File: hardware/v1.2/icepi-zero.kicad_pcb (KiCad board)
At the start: 4 copper layers, 65 x 30 mm, 158 parts, among them J1 Conn_02x20_Counter_Clockwise, J2 HDMI_C_1.3, J3 USB_C_Receptacle_USB2.0_14P, J4 USB_C_Receptacle_USB2.0_14P, J5 USB_C_Receptacle_USB2.0_14P, J6 Micro_SD_Card_Det2, SW1 SW_Push, SW2 SW_Push, U1 ECP5U_25F_CABGA256, U10 W9825G6KH, U11 W25Q128JVS, U2 TLV62569DBV, U3 TLV62569DBV, U4 TLV62569DBV, U5 PCA9306DC1, U6 FT231XQ, U7 TPD2EUSB30A, U8 TPD2EUSB30A, U9 TPD2EUSB30A, Y1 SITxxxxxx-1x-33E-50.000000

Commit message: Trying to document my journey :)
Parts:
- added R30: 27, Resistor_SMD:R_0201_0603Metric, F.Cu at (150.5, 117.3)
- added R33: 27, Resistor_SMD:R_0201_0603Metric, F.Cu at (150.5, 118.0)
- moved G*** 1.07 mm to (177.7, 99.8)
- moved LOGO1 0.83 mm to (169.2, 102.9)
- moved TP8 0.26 mm to (144.6, 118.4)
- renumbered C25 to C1, C9 to C10, C10 to C11, C11 to C12, C12 to C13, C13 to C14, C14 to C15, C15 to C16, C16 to C17, C17 to C18, C18 to C19, C1 to C2, C19 to C20, C20 to C21, C21 to C22, C22 to C23, C23 to C24, C24 to C25, C2 to C3, C3 to C4, C4 to C5, C5 to C6, C6 to C7, C7 to C8, C8 to C9, D7 to D10, D9 to D13, D10 to D14, D13 to D6, D14 to D7, D6 to D8, D8 to D9, R22 to R20, R23 to R21, R24 to R22, R25 to R23, R20 to R24, R21 to R25, R47 to R26, R48 to R27, R26 to R29, R27 to R31, R43 to R32, R40 to R34, R45 to R35, R29 to R36, R30 to R37, R41 to R38, R46 to R39, R42 to R40, R44 to R41, R39 to R42, R31 to R43, R32 to R44, R33 to R45, R34 to R46, R35 to R47, R36 to R48, R37 to R49, R38 to R50
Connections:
- net Net-(U9-D+) renamed /USB/D2A+
- net Net-(U9-D-) renamed /USB/D2A-
- J4 pad A6: D3+ -> /USB/D3A+
- J4 pad A7: D3- -> /USB/D3A-
- J4 pad B6: D3+ -> /USB/D3A+
- J4 pad B7: D3- -> /USB/D3A-
- R26 pad 2: D3- -> /USB/D3A-
- R27 pad 2: D3- -> /USB/D3A-
- R35 pad 2: D3+ -> /USB/D3A+
- R39 pad 2: D3+ -> /USB/D3A+
- U8 pad 1: D3+ -> /USB/D3A+
- U8 pad 2: D3- -> /USB/D3A-
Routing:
- net /USB/D3A+: track 0.00 -> 25.1 mm
- net /USB/D3A-: track 0.00 -> 24.5 mm
- net D3+: track 30.9 -> 8.88 mm
- net D3-: track 30.7 -> 8.78 mm
- net /USB/D2A+: track 13.3 -> 14.3 mm
- net GPDI_SCK: track 37.7 -> 38.4 mm
- net GPDI_SDA: track 38.1 -> 38.7 mm
- net +5V: track 163.1 -> 162.5 mm
- net GND: track 86.2 -> 86.4 mm, vias 109 -> 110
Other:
- board text added: "1"
- board text added: "2"
- board text removed: "USB1"
- board text removed: "USB2"

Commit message: Custom ECP5-CABGA256 symbol
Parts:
- U1: value ECP5U_25F_CABGA256 -> ECP5-CABGA256
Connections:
- net /ECP5/DBG1 renamed /DBG1
- net /ECP5/DBG2 renamed /DBG2
- net /GPIO/CONN_CK+ renamed /GPDI/CONN_CK+
- net /GPIO/CONN_CK- renamed /GPDI/CONN_CK-
- net /GPIO/CONN_D0+ renamed /GPDI/CONN_D0+
- net /GPIO/CONN_D0- renamed /GPDI/CONN_D0-
- net /GPIO/CONN_D1+ renamed /GPDI/CONN_D1+
- net /GPIO/CONN_D1- renamed /GPDI/CONN_D1-
- net /GPIO/CONN_D2+ renamed /GPDI/CONN_D2+
- net /GPIO/CONN_D2- renamed /GPDI/CONN_D2-
- net /GPIO/GPDI_SCK_5V renamed /GPDI/GPDI_SCK_5V
- net /GPIO/GPDI_SDA_5V renamed /GPDI/GPDI_SDA_5V
- net /USB/D2A+ renamed /USB/D0A+
- net /USB/D2A- renamed /USB/D0A-
- net /USB/D3A+ renamed /USB/D1A+
- net /USB/D3A- renamed /USB/D1A-
- net A0 renamed /SDRAM/A0
- net A1 renamed /SDRAM/A1
- net A10 renamed /SDRAM/A10
- net A11 renamed /SDRAM/A11
- net A12 renamed /SDRAM/A12
- net A2 renamed /SDRAM/A2
- net A3 renamed /SDRAM/A3
- net A4 renamed /SDRAM/A4
- net A5 renamed /SDRAM/A5
- net A6 renamed /SDRAM/A6
- net A7 renamed /SDRAM/A7
- net A8 renamed /SDRAM/A8
- net A9 renamed /SDRAM/A9
- net BA0 renamed /SDRAM/BA0
- net BA1 renamed /SDRAM/BA1
- net CKE renamed /SDRAM/CKE
- net CLK renamed /SDRAM/CLK
- net D0 renamed /SDRAM/D0
- net D1 renamed /SDRAM/D1
- net D1+ renamed /USB/D2+
- net D1- renamed /USB/D2-
- net D10 renamed /SDRAM/D10
- net D11 renamed /SDRAM/D11
- net D12 renamed /SDRAM/D12
- net D13 renamed /SDRAM/D13
- net D14 renamed /SDRAM/D14
- net D15 renamed /SDRAM/D15
- net D2 renamed /SDRAM/D2
- net D2+ renamed /USB/D0+
- net D2- renamed /USB/D0-
- net D3 renamed /SDRAM/D3
- net D3+ renamed /USB/D1+
- net D3- renamed /USB/D1-
- net D4 renamed /SDRAM/D4
- net D5 renamed /SDRAM/D5
- net D6 renamed /SDRAM/D6
- net D7 renamed /SDRAM/D7
- net D8 renamed /SDRAM/D8
- net D9 renamed /SDRAM/D9
- net DQM0 renamed /SDRAM/DQM0
- net DQM1 renamed /SDRAM/DQM1
- net FLASH_CLK renamed /Flash/FLASH_CLK
- net GLOBAL_CLK renamed /GLOBAL_CLK
- net GPDI_CEC renamed /GPDI/GPDI_CEC
- net GPDI_CLK+ renamed /GPDI/GPDI_CLK+
- net GPDI_CLK- renamed /GPDI/GPDI_CLK-
- net GPDI_D0+ renamed /GPDI/GPDI_D0+
- net GPDI_D0- renamed /GPDI/GPDI_D0-
- net GPDI_D1+ renamed /GPDI/GPDI_D1+
- net GPDI_D1- renamed /GPDI/GPDI_D1-
- net GPDI_D2+ renamed /GPDI/GPDI_D2+
- net GPDI_D2- renamed /GPDI/GPDI_D2-
- net GPDI_HPD renamed /GPDI/GPDI_HPD
- net GPDI_SCK renamed /GPDI/GPDI_SCK_3V3
- net GPDI_SDA renamed /GPDI/GPDI_SDA_3V3
- net GPDI_UTIL renamed /GPDI/GPDI_UTIL
- net GPIO_10 renamed /GPIO4
- net GPIO_11 renamed /GPIO5
- net GPIO_12 renamed /GPIO6
- net GPIO_13 renamed /GPIO7
- net GPIO_15 renamed /GPIO8
- net GPIO_16 renamed /GPIO9
- net GPIO_18 renamed /GPIO10
- net GPIO_19 renamed /GPIO11
- net GPIO_21 renamed /GPIO12
- net GPIO_22 renamed /GPIO13
- net GPIO_23 renamed /GPIO14
- net GPIO_24 renamed /GPIO15
- net GPIO_26 renamed /GPIO16
- net GPIO_27 renamed /GPIO17
- net GPIO_28 renamed /GPIO18
- net GPIO_29 renamed /GPIO19
- net GPIO_3 renamed /GPIO0
- net GPIO_31 renamed /GPIO20
- net GPIO_32 renamed /GPIO21
- net GPIO_33 renamed /GPIO22
- net GPIO_35 renamed /GPIO23
- net GPIO_36 renamed /GPIO24
- net GPIO_37 renamed /GPIO25
- net GPIO_38 renamed /GPIO26
- net GPIO_40 renamed /GPIO27
- net GPIO_5 renamed /GPIO1
- net GPIO_7 renamed /GPIO2
- net GPIO_8 renamed /GPIO3
- net LED1 renamed /LED0
- net LED2 renamed /LED1
- net LED3 renamed /LED2
- net LED4 renamed /LED3
- net LED5 renamed /LED4
- net SD_CLK renamed /uSD/SD_CLK
- net SD_CMD renamed /uSD/SD_CMD
- net SD_DAT0 renamed /uSD/SD_DAT0
- net SD_DAT1 renamed /uSD/SD_DAT1
- net SD_DAT2 renamed /uSD/SD_DAT2
- net SD_DAT3 renamed /uSD/SD_DAT3
- net SD_DET renamed /uSD/SD_DET
- net SW1 renamed /SW0
- net SW2 renamed /SW1
- net USB2_PULL_D+ renamed /USB/USB0_PULL_D+
- net USB2_PULL_D- renamed /USB/USB0_PULL_D-
- net USB3_PULL_D+ renamed /USB/USB1_PULL_D+
- net USB3_PULL_D- renamed /USB/USB1_PULL_D-
- net USB_RXD renamed /USB/USB_RXD
- net USB_TXD renamed /USB/USB_TXD
- net ~{CAS} renamed /SDRAM/~{CAS}
- net ~{CS} renamed /SDRAM/~{CS}
- net ~{RAS} renamed /SDRAM/~{RAS}
- net ~{RXLED} renamed /USB/~{RXLED}
- net ~{USB_DTR} renamed /USB/~{USB_DTR}
- net ~{USB_RTS} renamed /USB/~{USB_RTS}
- net ~{WE} renamed /SDRAM/~{WE}

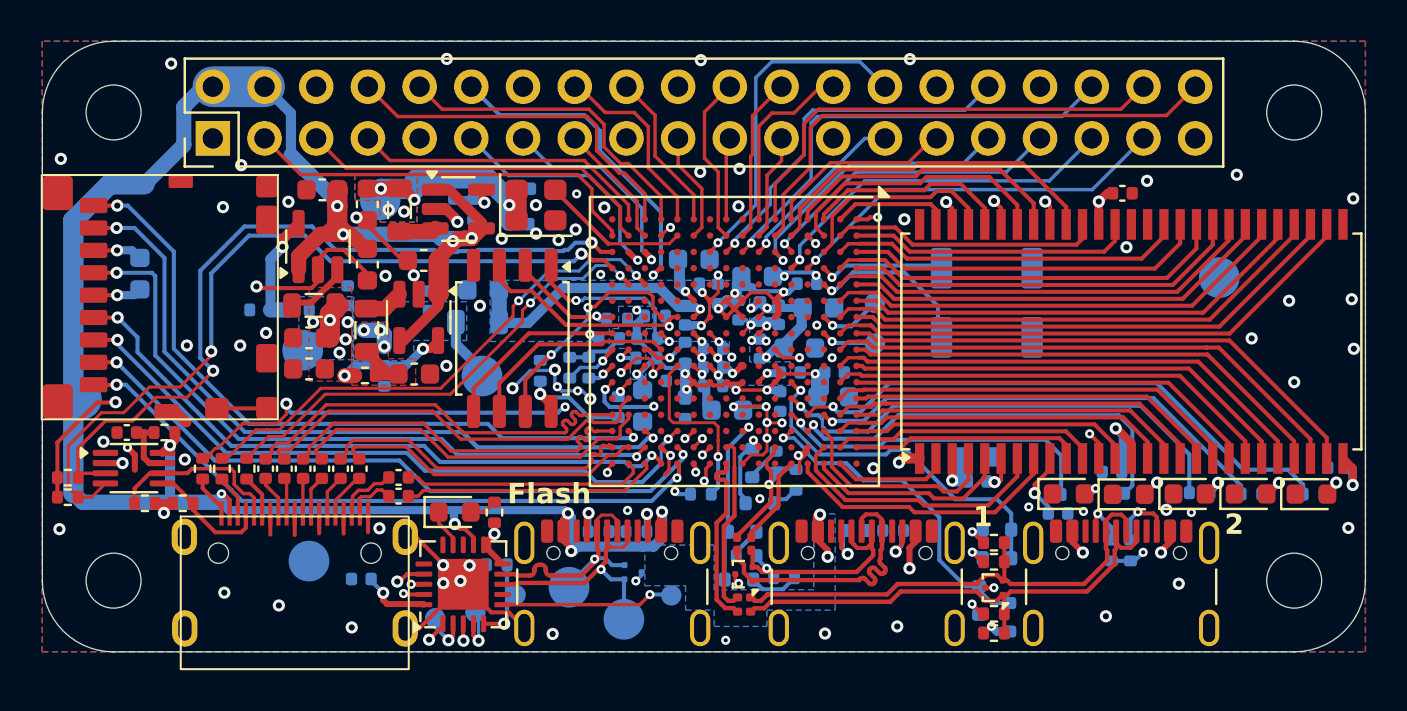
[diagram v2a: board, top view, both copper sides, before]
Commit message: Put better pin names for LPF files
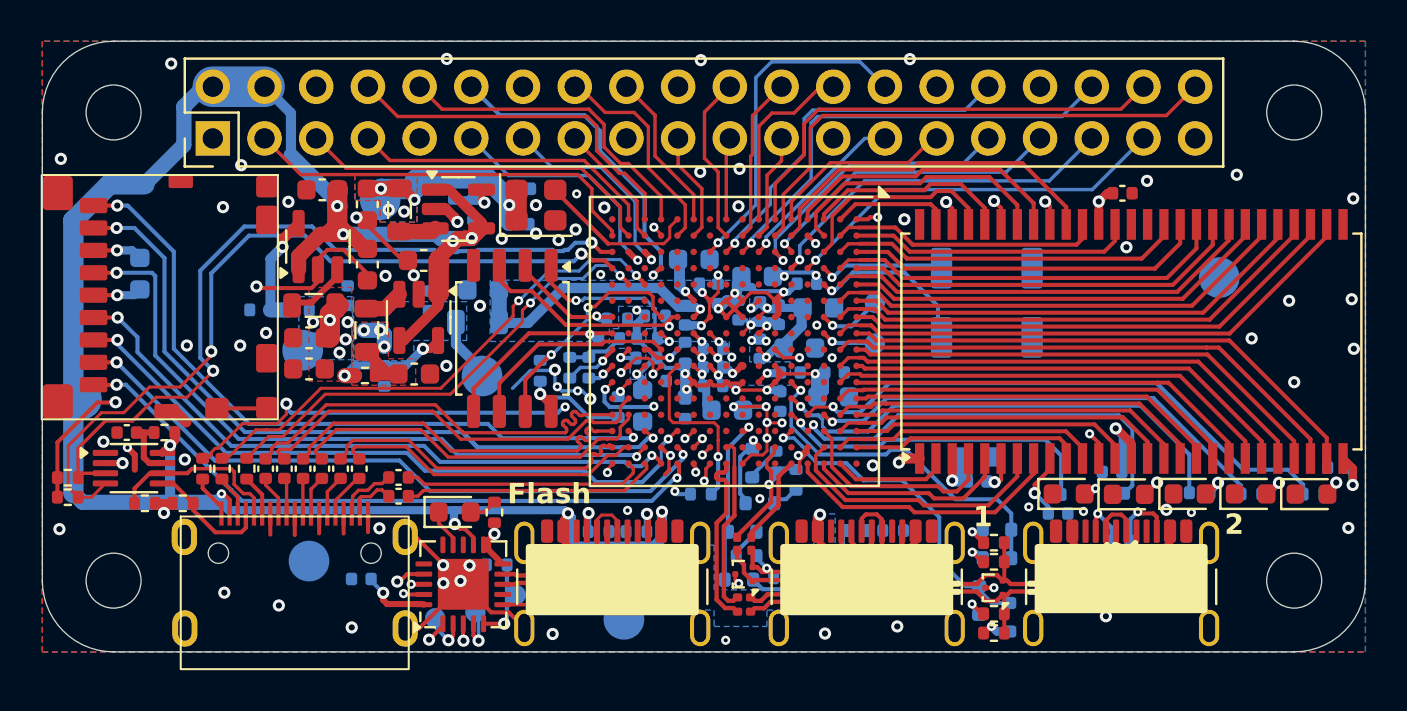
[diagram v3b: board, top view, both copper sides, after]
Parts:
- D8: value RED -> WHITE
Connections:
- U1 pad M1: /GPIO9 -> /GLOBAL_CLK
- U1 pad M2: /GLOBAL_CLK -> /GPIO9
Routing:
- net /GPIO9: track 9.34 -> 10.5 mm
- net /GLOBAL_CLK: track 7.17 -> 7.81 mm
- net /GPIO6: track 16.3 -> 16.8 mm
- net GND: track 86.4 -> 86.3 mm, vias 110 -> 109

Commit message: Don't overwrite v1.2 with v1.3
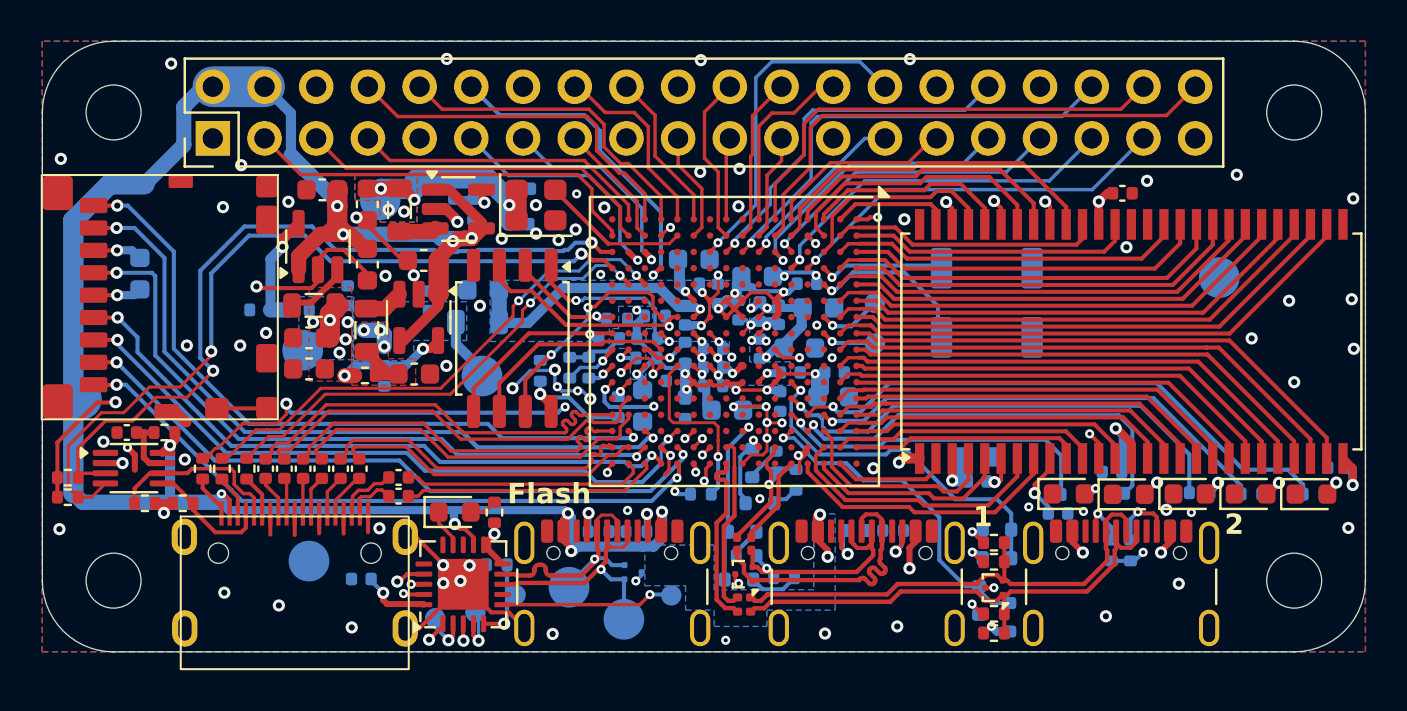
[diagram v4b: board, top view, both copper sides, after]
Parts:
- D8: value WHITE -> RED
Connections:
- U1 pad M1: /GLOBAL_CLK -> /GPIO9
- U1 pad M2: /GPIO9 -> /GLOBAL_CLK
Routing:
- net /GPIO9: track 10.5 -> 9.34 mm
- net /GLOBAL_CLK: track 7.81 -> 7.17 mm
- net /GPIO6: track 16.8 -> 16.3 mm
- net GND: track 86.3 -> 86.4 mm, vias 109 -> 110

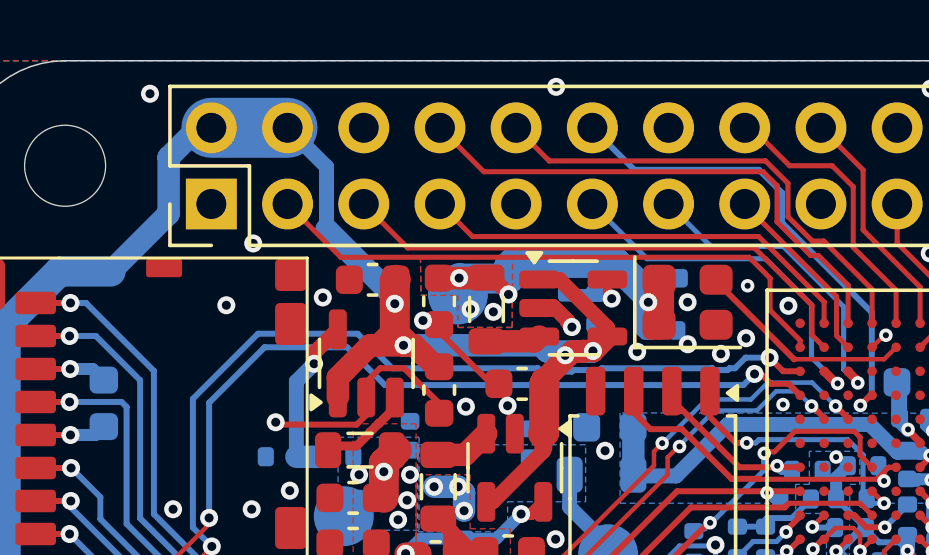
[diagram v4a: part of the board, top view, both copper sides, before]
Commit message: Add wip uart 2 ps2 converter
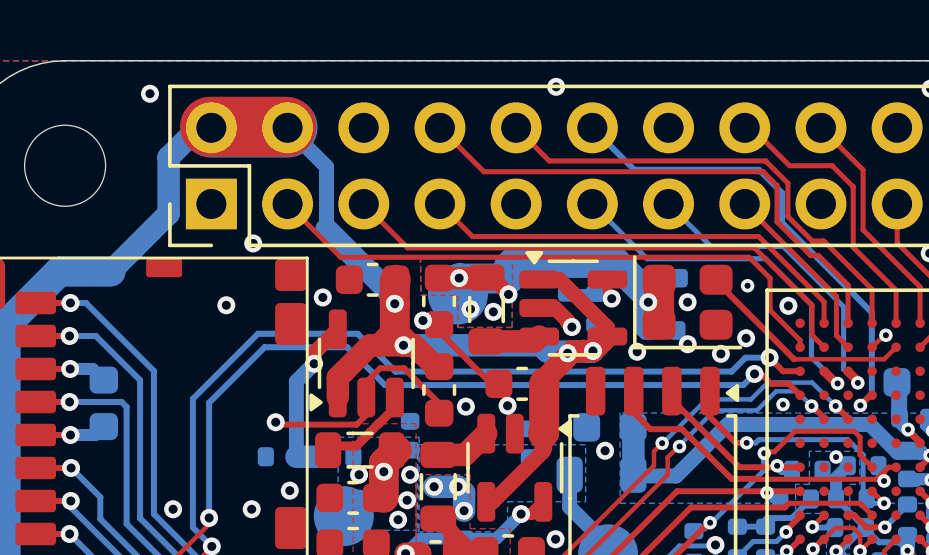
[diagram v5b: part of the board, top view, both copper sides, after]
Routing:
- net +5V: track 162.5 -> 165.1 mm
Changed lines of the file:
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@@
 	)
 	(segment
-		(start 141.6 113.472461)
-		(end 141.6 114.07)
-		(width 0.3)
+		(start 136.410199 99.693323)
+		(end 136.727631 99.693323)
+		(width 0.75)
 		(layer "F.Cu")
 		(net 19)
 	)
 	(segment
-		(start 137.095 99.675)
-		(end 137.5775 99.1925)
-		(width 0.75)
+		(start 141.6 113.472461)
+		(end 141.6 114.07)
+		(width 0.3)
 		(layer "F.Cu")
 		(net 19)
@@
 	)
 	(segment
-		(start 136.731258 99.693323)
-		(end 136.410199 99.693323)
-		(width 0.75)
-		(layer "F.Cu")
-		(net 19)
-	)
-	(segment
 		(start 158.6 115.9)
 		(end 158.6 114.89)
@@
 	)
 	(segment
-		(start 136.749581 99.675)
-		(end 136.731258 99.693323)
-		(width 0.75)
-		(layer "F.Cu")
-		(net 19)
-	)
-	(segment
 		(start 128.801251 100.351251)
 		(end 129.667 99.485501)
@@
 	)
 	(segment
+		(start 136.745954 99.675)
+		(end 137.095 99.675)
+		(width 0.75)
+		(layer "F.Cu")
+		(net 19)
+	)
+	(segment
 		(start 137.17 114.37)
 		(end 137.17 114.7425)
@@
 	)
 	(segment
-		(start 136.410199 99.693323)
-		(end 135.485 100.618522)
-		(width 0.75)
-		(layer "F.Cu")
-		(net 19)
-	)
-	(segment
 		(start 141.82276 113.249701)
 		(end 141.6 113.472461)
@@
 	)
 	(segment
-		(start 137.095 99.675)
-		(end 136.749581 99.675)
+		(start 135.485 100.618522)
+		(end 135.485 100.77)
 		(width 0.75)
 		(layer "F.Cu")
@@
 	)
 	(segment
+		(start 136.410199 99.693323)
+		(end 135.485 100.618522)
+		(width 0.75)
+		(layer "F.Cu")
+		(net 19)
+	)
+	(segment
 		(start 154.207 113.257)
 		(end 154.1 113.364)
@@
 	)
 	(segment
-		(start 135.485 100.618522)
-		(end 135.485 100.77)
-		(width 0.75)
+		(start 126.87 92.2)
+		(end 124.33 92.2)
+		(width 2)
 		(layer "F.Cu")
 		(net 19)
@@
 	)
 	(segment
+		(start 136.727631 99.693323)
+		(end 136.745954 99.675)
+		(width 0.75)
+		(layer "F.Cu")
+		(net 19)
+	)
+	(segment
 		(start 171.4 114.608281)
 		(end 170.96 115.048281)
@@
 	)
 	(segment
+		(start 137.095 99.675)
+		(end 137.5775 99.1925)
+		(width 0.75)
+		(layer "F.Cu")
+		(net 19)
+	)
+	(segment
 		(start 121.975 112.7)
 		(end 122.39 112.7)
@@
 	)
 	(via
-		(at 136.17 99.82)
+		(at 136.25 99.75)
 		(size 0.6)
 		(drill 0.3)
@@
 	)
 	(segment
+		(start 126.915 92.225)
+		(end 124.375 92.225)
+		(width 2)
+		(layer "B.Cu")
+		(net 19)
+	)
+	(segment
 		(start 145.49 114.826512)
 		(end 146.031106 114.826512)
@@
 	)
 	(segment
-		(start 126.915 92.235)
-		(end 124.375 92.235)
-		(width 2)
-		(layer "B.Cu")
-		(net 19)
-	)
-	(segment
 		(start 130.780501 99.485501)
 		(end 135.365501 99.485501)
@@
 	)
 	(segment
-		(start 135.258844 100.25)
-		(end 130.4 100.25)
-		(width 0.2)
-		(layer "B.Cu")
-		(net 115)
-	)
-	(segment
-		(start 135.318167 100.309323)
-		(end 135.258844 100.25)
-		(width 0.2)
-		(layer "B.Cu")
-		(net 115)
-	)
-	(segment
-		(start 135.94591 100.361)
-		(end 135.894233 100.309323)
-		(width 0.2)
-		(layer "B.Cu")
-		(net 115)
-	)
-	(segment
-		(start 129.25 99.1)
-		(end 125.93 99.1)
-		(width 0.2)
-		(layer "B.Cu")
-		(net 115)
-	)
-	(segment
-		(start 142.983162 99.896838)
-		(end 142.183162 99.896838)
-		(width 0.2)
-		(layer "B.Cu")
-		(net 115)
-	)
-	(segment
-		(start 141.13591 100.311)
-		(end 141.07491 100.25)
-		(width 0.2)
-		(layer "B.Cu")
-		(net 115)
-	)
-	(segment
-		(start 136.39409 100.361)
-		(end 135.94591 100.361)
-		(width 0.2)
-		(layer "B.Cu")
-		(net 115)
-	)
-	(segment
-		(start 123.76 101.27)
-		(end 123.76 105.56)
-		(width 0.2)
-		(layer "B.Cu")
-		(net 115)
-	)
-	(segment
-		(start 135.894233 100.309323)
-		(end 135.318167 100.309323)
-		(width 0.2)
-		(layer "B.Cu")
-		(net 115)
-	)
-	(segment
-		(start 136.445767 100.309323)
-		(end 136.39409 100.361)
+		(start 141.719 100.361)
+		(end 130.511 100.361)
 		(width 0.2)
 		(layer "B.Cu")
@@
 	(segment
 		(start 142.183162 99.896838)
-		(end 141.83 100.25)
-		(width 0.2)
-		(layer "B.Cu")
-		(net 115)
-	)
-	(segment
-		(start 130.4 100.25)
-		(end 129.25 99.1)
-		(width 0.2)
-		(layer "B.Cu")
-		(net 115)
-	)
-	(segment
-		(start 141.07491 100.25)
-		(end 137.391156 100.25)
-		(width 0.2)
-		(layer "B.Cu")
-		(net 115)
-	)
-	(segment
-		(start 137.391156 100.25)
-		(end 137.331833 100.309323)
+		(end 141.719 100.361)
 		(width 0.2)
 		(layer "B.Cu")
@@
 	)
 	(segment
-		(start 141.64509 100.25)
-		(end 141.58409 100.311)
+		(start 142.983162 99.896838)
+		(end 142.183162 99.896838)
 		(width 0.2)
 		(layer "B.Cu")
@@
 	)
 	(segment
-		(start 141.58409 100.311)
-		(end 141.13591 100.311)
+		(start 129.25 99.1)
+		(end 125.93 99.1)
 		(width 0.2)
 		(layer "B.Cu")
@@
 	)
 	(segment
-		(start 137.331833 100.309323)
-		(end 136.445767 100.309323)
+		(start 123.76 101.27)
+		(end 123.76 105.56)
 		(width 0.2)
 		(layer "B.Cu")
@@
 	)
 	(segment
-		(start 141.83 100.25)
-		(end 141.64509 100.25)
+		(start 130.511 100.361)
+		(end 129.25 99.1)
 		(width 0.2)
 		(layer "B.Cu")
